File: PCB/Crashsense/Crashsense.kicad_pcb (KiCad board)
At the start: 2 copper layers, 49 parts, among them J1 u-blox NEO-M8N, J2 Micro_SD_Card_Det1, J3 BATTERY_CONNECTOR, J4 Debug_pins, P1 USB_C_Plug_USB2.0, SW1 SW_Push, SW2 SW_Push, U1 ESP32-S3-WROOM-1, U2 ADXL377, U3 BMM150, U4 DS3231M, U5 BMI270, U6 TP4056-42-ESOP8, U7 ME6211C10M5

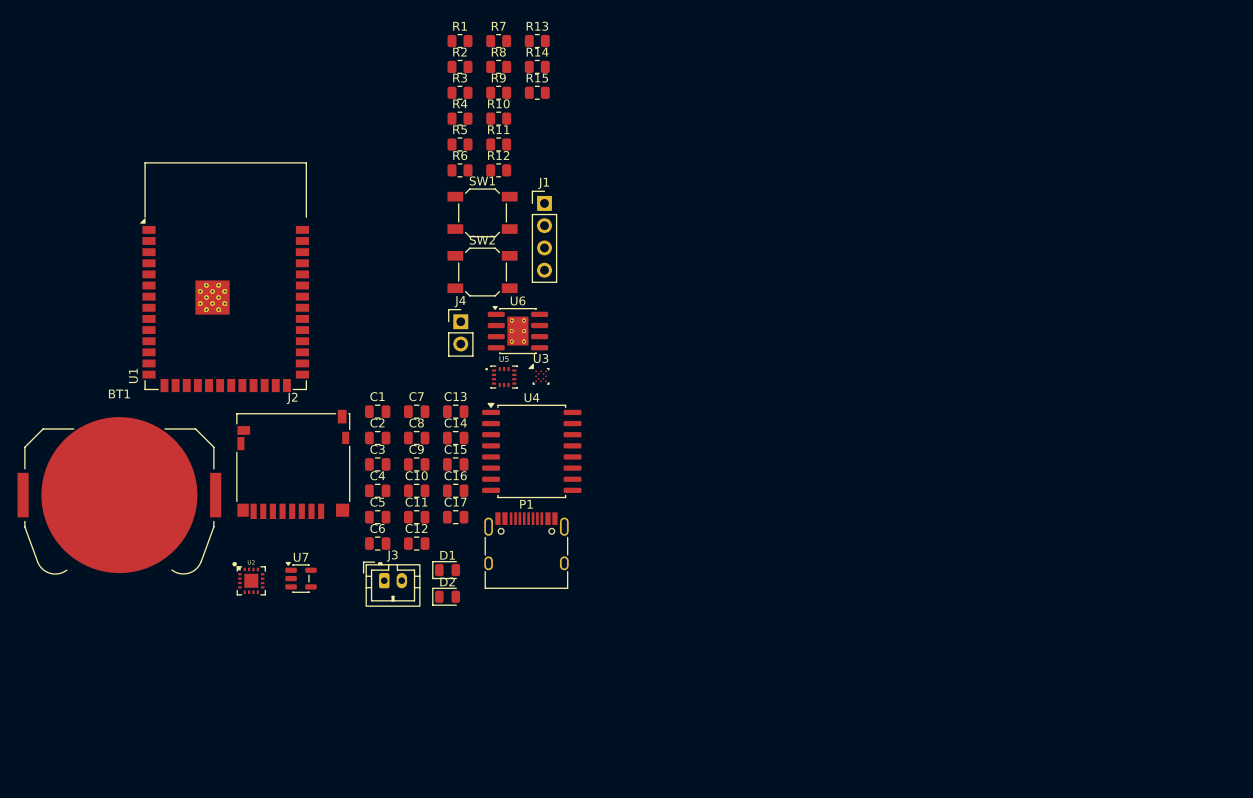
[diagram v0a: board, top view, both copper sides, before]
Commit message: Finished PCB componen placement and journalling
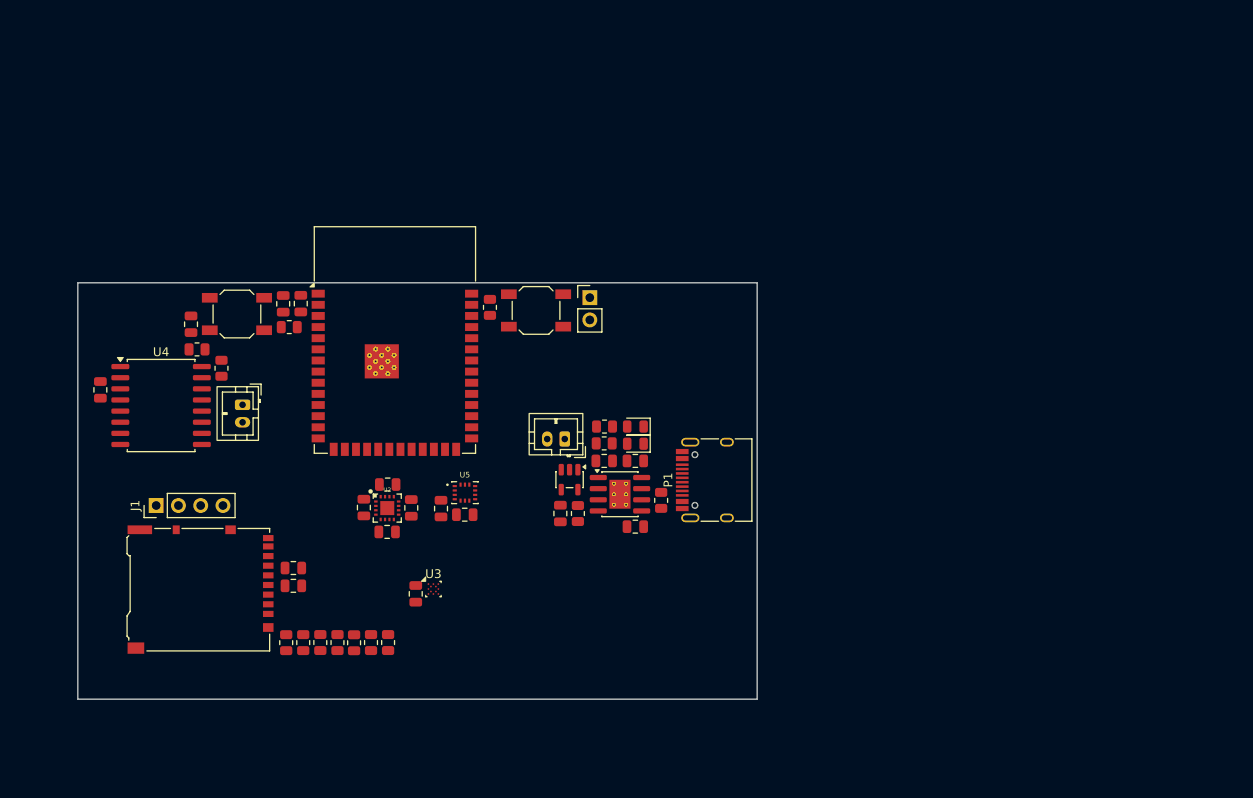
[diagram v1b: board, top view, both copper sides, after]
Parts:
- removed BT1: Battery_Cell, Battery:BatteryHolder_Keystone_3034_1x20mm
- added J5: Coincell_BAT, Connector_JST:JST_PH_B2B-PH-K_1x02_P2.00mm_Vertical, F.Cu at (129.8, 93.4)
- J2: footprint Connector_Card:microSD_HC_Hirose_DM3D-SF -> Connector_Card:microSD_HC_Hirose_DM3AT-SF-PEJM5
- moved R7 71.6 mm to (138.7, 120.5), turned to -90 degrees
- moved R8 69.4 mm to (136.7, 120.5), turned to -90 degrees
- moved R9 67.3 mm to (134.8, 120.6), turned to -90 degrees
- moved R10 61.5 mm to (144.4, 120.5), turned to -90 degrees
- moved R11 58.2 mm to (146.4, 120.5), turned to -90 degrees
- moved R5 58.1 mm to (142.5, 120.6), turned to -90 degrees
- moved R1 57.2 mm to (177.6, 104.3), turned to 90 degrees
- moved J1 56.1 mm to (119.9, 104.9), turned to 90 degrees
- moved R6 55.7 mm to (140.6, 120.5), turned to -90 degrees
- moved R2 52.7 mm to (168.1, 105.8), turned to -90 degrees
- moved R13 52.4 mm to (124.6, 87.1), turned to 180 degrees
- moved R3 43.3 mm to (171.1, 97.8)
- moved U4 42.6 mm to (120.5, 93.5)
- moved R14 41.0 mm to (135.1, 84.6)
- moved C11 38.9 mm to (113.6, 91.7), turned to -90 degrees
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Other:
- board outline added: 77.5 x 47.5 mm

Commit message: jopurnal for today
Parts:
- moved R1 0.59 mm to (177.6, 104.9)
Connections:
- J1 pad 3: GPS_TX -> GPS_RX
- J1 pad 4: GPS_RX -> GPS_TX
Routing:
- net GND: track 0.00 -> 127.1 mm, vias 0 -> 33
- net 3V3: track 0.00 -> 62.7 mm, vias 0 -> 21
- net I2C_SCL: track 0.00 -> 56.8 mm, vias 0 -> 9
- net USB_D+: track 0.00 -> 51.1 mm, vias 0 -> 2
- net USB_D-: track 0.00 -> 50.5 mm, vias 0 -> 2
- net +5V_USB: track 0.00 -> 41.2 mm, vias 0 -> 2
- net I2C_SDA: track 0.00 -> 38.9 mm, vias 0 -> 2
- net SD_MISO: track 0.00 -> 35.7 mm, vias 0 -> 2
- net SD_SCK: track 0.00 -> 35.5 mm, vias 0 -> 4
- net SD_MOSI: track 0.00 -> 31.9 mm, vias 0 -> 3
- net SD_DET: track 0.00 -> 31.5 mm
- net SD_CS: track 0.00 -> 29.8 mm, vias 0 -> 2
- net VBAT: track 0.00 -> 24.7 mm, vias 0 -> 2
- net GPS_RX: track 0.00 -> 18.7 mm
- net DAT1: track 0.00 -> 16.9 mm
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- added copper zone on In2.Cu, net 3V3
- added copper zone on In1.Cu, net GND
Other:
- copper layers 2 -> 4

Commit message: PCb rerouting started and journalled for today
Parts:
- added REF**: MountingHole_3.2mm_M3, MountingHole:MountingHole_3.2mm_M3, F.Cu at (151.0, 132.5)
- added REF**: MountingHole_3.2mm_M3, MountingHole:MountingHole_3.2mm_M3, F.Cu at (239.0, 132.5)
- added REF**: MountingHole_3.2mm_M3, MountingHole:MountingHole_3.2mm_M3, F.Cu at (239.0, 80.5)
- added REF**: MountingHole_3.2mm_M3, MountingHole:MountingHole_3.2mm_M3, F.Cu at (151.0, 80.5)
- moved J1 109.1 mm to (227.5, 86.5), turned to 0 degrees
- moved J3 71.7 mm to (238.1, 92.0), turned to -90 degrees
- moved C14 64.7 mm to (212.8, 128.2)
- moved U3 64.7 mm to (214.9, 127.7)
- moved C10 59.4 mm to (200.0, 128.0), turned to -90 degrees
- moved C9 57.4 mm to (197.4, 125.3), turned to 0 degrees
- moved U2 55.9 mm to (197.3, 127.9), turned to -90 degrees
- moved C1 55.0 mm to (229.6, 103.0)
- moved C2 55.0 mm to (229.6, 110.5)
- moved U6 55.0 mm to (227.8, 106.8)
- moved U7 55.0 mm to (222.1, 105.1)
- moved C3 55.0 mm to (226.0, 103.0)
- moved C4 55.0 mm to (221.0, 109.0)
- moved D1 55.0 mm to (229.6, 101.0)
- moved D2 55.0 mm to (229.6, 99.1)
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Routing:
- net 3V3: track 62.7 -> 0.00 mm, vias 21 -> 0
- net GND: track 127.1 -> 66.7 mm, vias 33 -> 45
- net I2C_SCL: track 56.8 -> 0.00 mm, vias 9 -> 0
- net USB_D+: track 51.1 -> 0.00 mm, vias 2 -> 0
- net USB_D-: track 50.5 -> 0.00 mm, vias 2 -> 0
- net +5V_USB: track 41.2 -> 0.00 mm, vias 2 -> 0
- net I2C_SDA: track 38.9 -> 0.00 mm, vias 2 -> 0
- net SD_MISO: track 35.7 -> 0.00 mm, vias 2 -> 0
- net SD_SCK: track 35.5 -> 0.00 mm, vias 4 -> 0
- net SD_MOSI: track 31.9 -> 0.00 mm, vias 3 -> 0
- net SD_DET: track 31.5 -> 0.00 mm
- net SD_CS: track 29.8 -> 0.00 mm, vias 2 -> 0
- net VBAT: track 24.7 -> 0.00 mm, vias 2 -> 0
- net GPS_RX: track 18.7 -> 0.00 mm
- net DAT1: track 16.9 -> 0.00 mm
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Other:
- board size 77.5 x 47.5 mm -> 96 x 59.8 mm

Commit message: PCb finished and journalled for today
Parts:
- added ?: , clipboard:f59ac847-f748-4106-ba1d-d1278d51b1ea, B.Cu at (162.9, 124.2)
- added G***: LOGO, hackclublogo:hackclublogo, F.Cu at (232.0, 121.5)
- added G***: LOGO, LOGO, F.Cu at (206.0, 110.0)
- RTC : renamed from U4
- u-blox NEO-M8N: renamed from J1
- moved R12 2.99 mm to (168.9, 87.3), turned to 180 degrees
- moved R13 2.73 mm to (170.1, 90.0), turned to -90 degrees
- moved C10 0.25 mm to (200.3, 128.0)
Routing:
- net I2C_SDA: track 0.00 -> 101.9 mm, vias 0 -> 2
- net I2C_SCL: track 0.00 -> 90.4 mm, vias 0 -> 2
- net USB_D-: track 0.00 -> 57.3 mm, vias 0 -> 2
- net USB_D+: track 0.00 -> 57.2 mm, vias 0 -> 2
- net ACCEL_Z: track 0.00 -> 53.3 mm, vias 0 -> 6
- net ACCEL_X: track 0.00 -> 51.8 mm, vias 0 -> 4
- net ACCEL_Y: track 0.00 -> 51.7 mm, vias 0 -> 6
- net 3V3: track 0.00 -> 47.7 mm, vias 0 -> 28
- net VBAT: track 0.00 -> 44.3 mm, vias 0 -> 4
- net GPS_TX: track 0.00 -> 42.2 mm, vias 0 -> 2
- net GPS_RX: track 0.00 -> 42.2 mm, vias 0 -> 2
- net SD_MISO: track 0.00 -> 41.6 mm, vias 0 -> 4
- net SD_DET: track 0.00 -> 40.7 mm, vias 0 -> 2
- net SD_SCK: track 0.00 -> 39.7 mm, vias 0 -> 4
- net SD_MOSI: track 0.00 -> 37.3 mm, vias 0 -> 2
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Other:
- board size 96 x 59.8 mm -> 96 x 60 mm
- board text added: "7/29/2026"
- board text added: "CRASHSENSE MARK- I"
- board text added: "Designed By Parth Dhiman"
- board text added: "EN"
- board text added: "IO0"
- board text added: "Micro SD Card conn"
- board text added: "Power System"
- board text added: "Sensor Node"
